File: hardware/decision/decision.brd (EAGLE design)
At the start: 45 x 70 mm, 8 parts, among them IC1 7805T, IC2 A1301UA

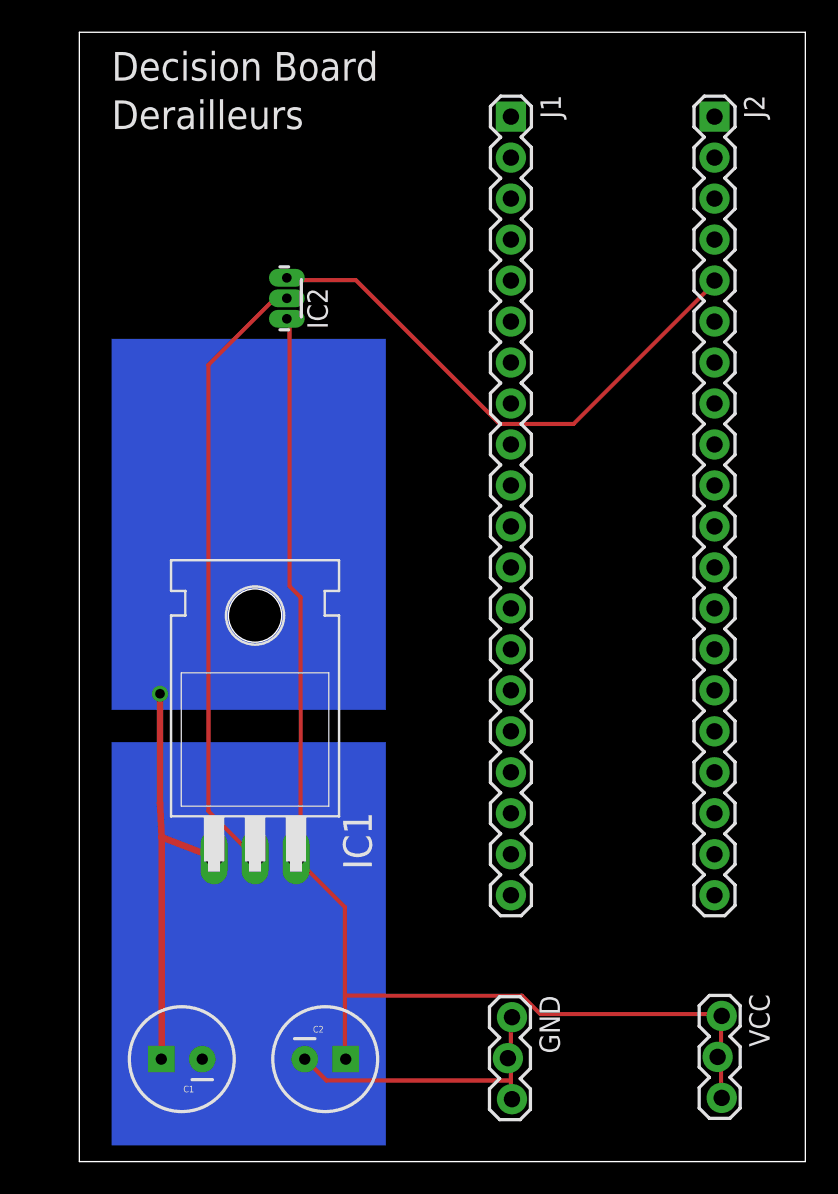
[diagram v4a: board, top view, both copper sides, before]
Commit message: Finish routing all boards, schematics are consitant, and all deliverable requirements are met..
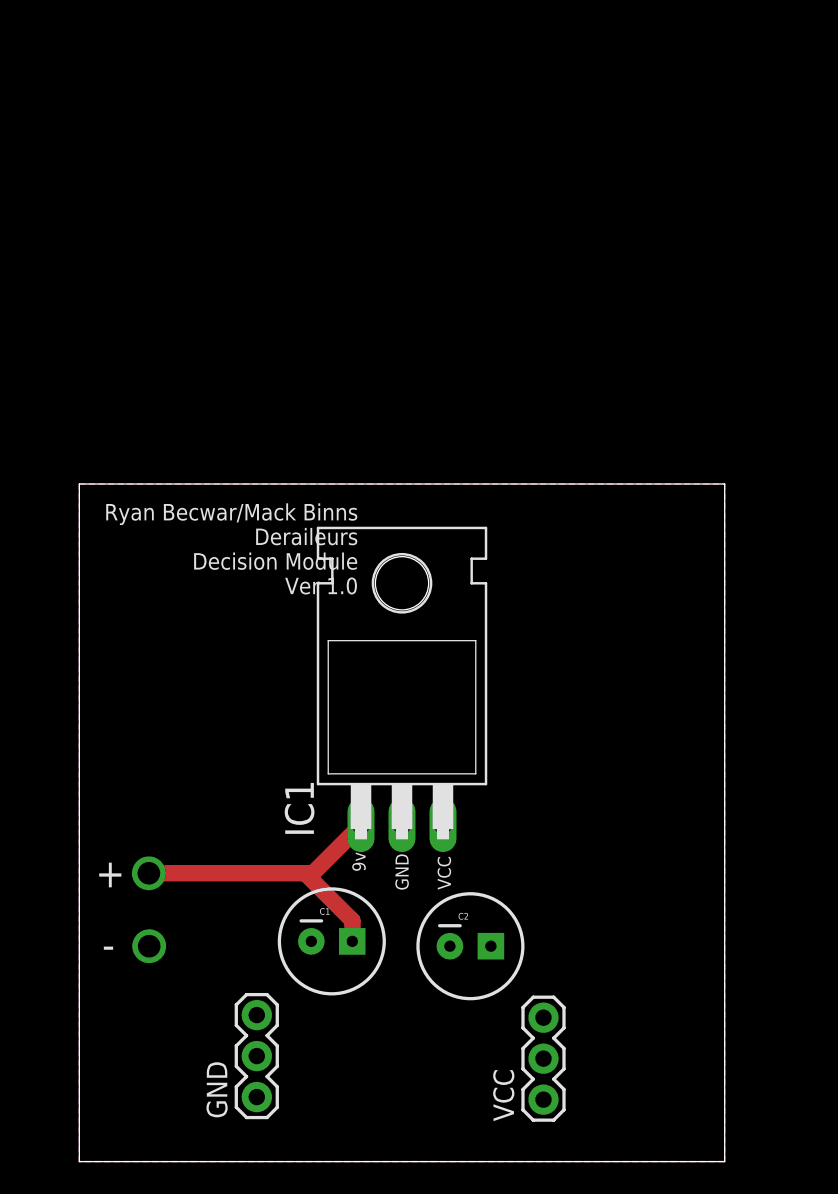
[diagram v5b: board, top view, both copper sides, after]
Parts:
- removed IC2: A1301UA, allegro:SIP3-UA
- removed J1, J2: (no value), SparkFun-Connectors:1X20
- GND: value (none) -> 0v; device SparkFun-Connectors:1X03_LOCK -> SparkFun-Connectors:1X03
- VCC: value (none) -> 5v; device SparkFun-Connectors:1X03_LOCK -> SparkFun-Connectors:1X03
- moved GND 16.5 mm to (11.0, 4.00), turned to 90 degrees
- moved VCC 12.1 mm to (28.8, 3.84), turned to 90 degrees
- moved C1 11.8 mm to (15.7, 13.7), turned to 0 degrees
- moved C2 11.4 mm to (24.2, 13.3)
- moved IC1 9.33 mm to (20.0, 31.0)
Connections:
- removed net P1.2: IC2.3, J2.5
- net GND: no longer IC2.2
- net VCC: no longer IC2.1
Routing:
- net VCC: track 76.9 -> 0.00 mm
- net GND: track 75.4 -> 0.00 mm, vias 0 -> 1
- net P1.2: track 34.0 -> 0.00 mm
- net 9V: track 26.1 -> 19.9 mm
- added copper zone on layer 16, net GND
- added copper zone on layer 1, net VCC
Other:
- board size 45 x 70 mm -> 40 x 42 mm
- board text added: "+"
- board text added: "-"
- board text added: "9v"
- board text added: "GND"
- board text added: "Ryan Becwar/Mack Binns Deraileurs Decision Module Ver 1.0"
- board text added: "VCC"
- board text removed: "Decision Board"
- board text removed: "Derailleurs"
